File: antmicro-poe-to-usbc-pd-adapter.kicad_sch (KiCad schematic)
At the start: 91 parts, among them J1 Bus_RJ45_5-2337992-8, J2 Bus_RJ45_5-2337992-8, J3 USB-C_GCT_USB4105-GF-A, Q1 PJE138K, U1 TPS2372-3RGWR, U2 LV14540DDAR, U3 INA230AIRGTR, U4 IEA48003A280V-001-R, U5 FT4232H_VQFN, U6 TPS65987DDHRSHR, U7 LV14540DDAR, Y1 Resonator_12MHz_ABM8G

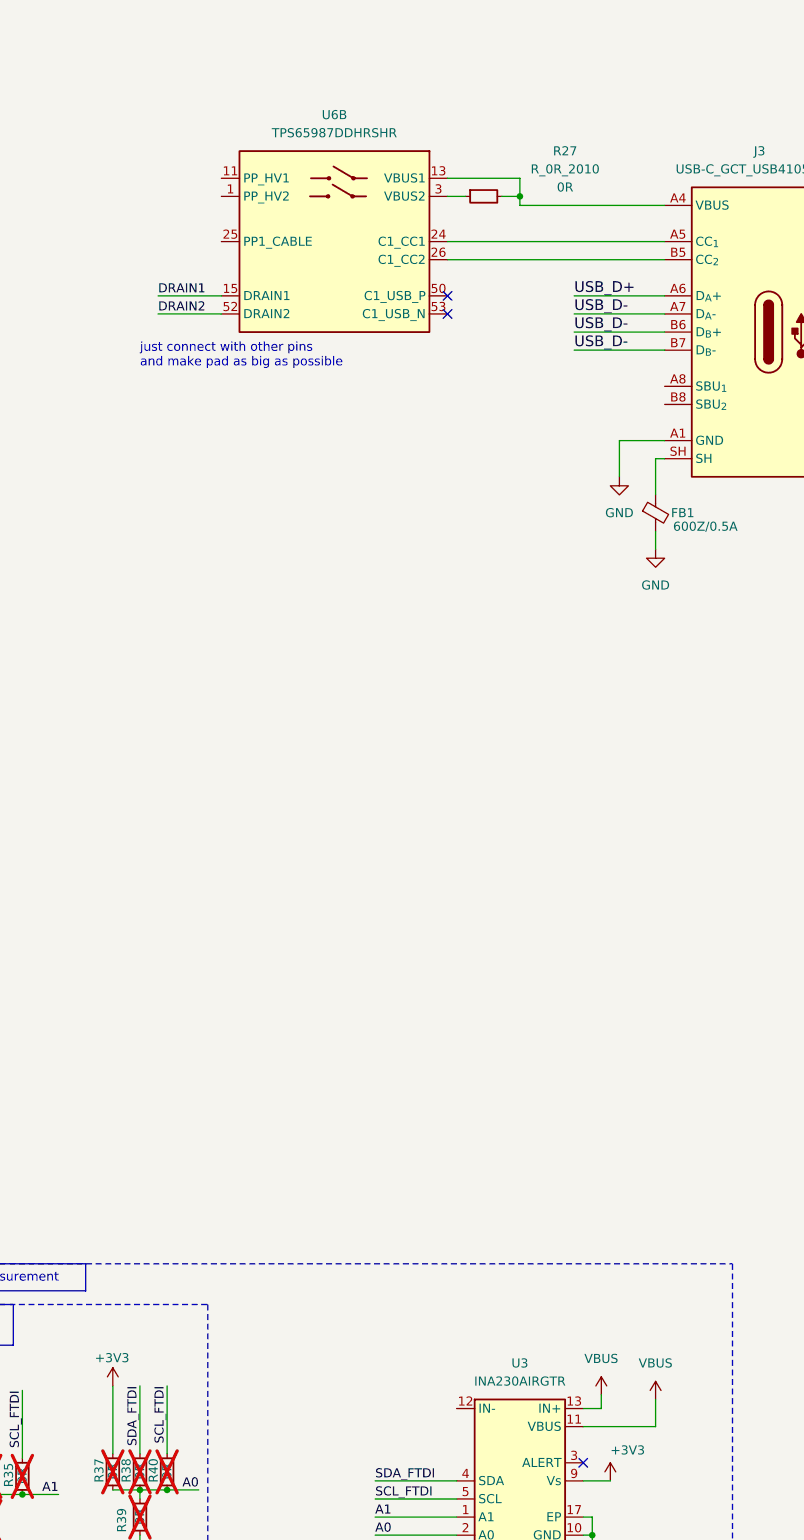
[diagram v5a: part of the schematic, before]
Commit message: [#62182] Add shunt resistor for INA230
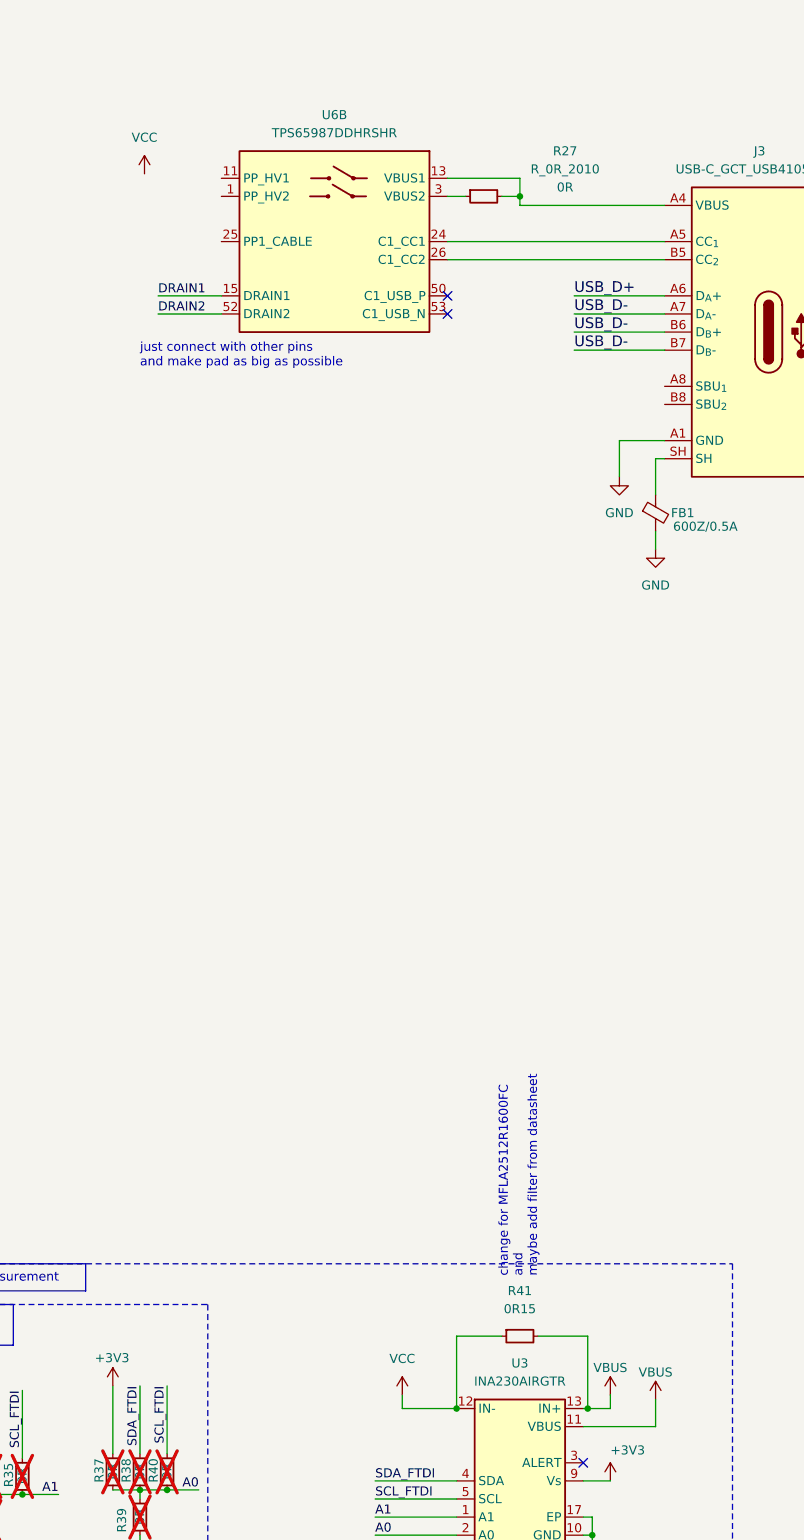
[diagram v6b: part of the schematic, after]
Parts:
- added R41: R_0R15_2010, antmicro-footprints:R_2010_5025Metric, symbol antmicroResistorsmisc:R_0R15_2010
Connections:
- net VBUS: now also R41.2
- net VCC: now reaches U3.12 (IN-)
- net VCC: now also R41.1
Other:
- note added: "change for MFLA2512R1600FC and maybe add filter from datasheet"
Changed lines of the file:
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@@
   (junction (at 367.03 111.125) (diameter 0) (color 0 0 0 0)
   )
+  (junction (at 358.14 281.305) (diameter 0) (color 0 0 0 0)
+  )
   (junction (at 133.35 353.06) (diameter 0) (color 0 0 0 0)
   )
@@
   (junction (at 189.23 361.95) (diameter 0) (color 0 0 0 0)
   )
+  (junction (at 376.555 281.305) (diameter 0) (color 0 0 0 0)
+  )
   (junction (at 133.35 379.73) (diameter 0) (color 0 0 0 0)
   )
@@
     (stroke (width 0) (type default))
   )
+  (wire (pts (xy 364.49 271.145) (xy 358.14 271.145))
+    (stroke (width 0) (type default))
+  )
   (wire (pts (xy 240.03 367.03) (xy 242.57 367.03))
     (stroke (width 0) (type default))
@@
     (stroke (width 0) (type default))
   )
+  (wire (pts (xy 376.555 281.305) (xy 379.73 281.305))
+    (stroke (width 0) (type default))
+  )
   (wire (pts (xy 292.735 299.72) (xy 292.735 300.99))
     (stroke (width 0) (type default))
@@
     (stroke (width 0) (type default))
   )
+  (wire (pts (xy 350.52 279.4) (xy 350.52 281.305))
+    (stroke (width 0) (type default))
+  )
   (wire (pts (xy 233.68 372.11) (xy 233.68 386.08))
     (stroke (width 0) (type default))
@@
     (stroke (width 0) (type default))
   )
+  (wire (pts (xy 358.14 271.145) (xy 358.14 281.305))
+    (stroke (width 0) (type default))
+  )
   (wire (pts (xy 115.57 334.01) (xy 123.19 334.01))
     (stroke (width 0) (type default))
@@
     (stroke (width 0) (type default))
   )
+  (wire (pts (xy 358.14 281.305) (xy 350.52 281.305))
+    (stroke (width 0) (type default))
+  )
   (wire (pts (xy 43.18 220.98) (xy 53.34 220.98))
     (stroke (width 0) (type default))
@@
     (stroke (width 0) (type default))
   )
-  (wire (pts (xy 378.46 279.4) (xy 378.46 281.305))
+  (wire (pts (xy 379.73 279.4) (xy 379.73 281.305))
     (stroke (width 0) (type default))
   )
@@
     (stroke (width 0) (type default))
   )
-  (wire (pts (xy 375.92 281.305) (xy 378.46 281.305))
+  (wire (pts (xy 375.92 281.305) (xy 376.555 281.305))
     (stroke (width 0) (type default))
   )
@@
     (stroke (width 0) (type default))
   )
+  (wire (pts (xy 376.555 281.305) (xy 376.555 271.145))
+    (stroke (width 0) (type default))
+  )
   (wire (pts (xy 27.94 332.74) (xy 27.94 328.93))
     (stroke (width 0) (type default))
@@
     (stroke (width 0) (type default))
   )
+  (wire (pts (xy 376.555 271.145) (xy 369.57 271.145))
+    (stroke (width 0) (type default))
+  )
   (wire (pts (xy 135.89 124.46) (xy 151.13 124.46))
     (stroke (width 0) (type default))
@@
     (effects (font (size 1.27 1.27)) (justify left bottom))
   )
+  (text "change for MFLA2512R1600FC\nand\nmaybe add filter from datasheet"
+    (at 369.57 262.89 90)
+    (effects (font (size 1.27 1.27)) (justify left bottom))
+  )
   (text "Nlogic same \nas Orin" (at 203.2 111.76 0)
     (effects (font (size 1.27 1.27)) (justify left bottom))
@@
     )
   )
-  (symbol (lib_id "antmicropower:VBUS") (at 378.46 279.4 0) (unit 1)
-    (in_bom yes) (on_board yes) (dnp no) (fields_autoplaced)
-    (property "Reference" "#PWR067" (at 378.46 283.21 0)
+  (symbol (lib_id "antmicropower:VBUS") (at 379.73 279.4 0) (unit 1)
+    (in_bom yes) (on_board yes) (dnp no)
+    (property "Reference" "#PWR067" (at 379.73 283.21 0)
       (effects (font (size 1.27 1.27)) hide)
     )
-    (property "Value" "VBUS" (at 378.46 274.32 0)
+    (property "Value" "VBUS" (at 379.73 275.59 0)
       (effects (font (size 1.27 1.27)))
     )
-    (property "Footprint" "" (at 378.46 279.4 0)
+    (property "Footprint" "" (at 379.73 279.4 0)
       (effects (font (size 1.27 1.27)) hide)
     )
-    (property "Datasheet" "" (at 378.46 279.4 0)
+    (property "Datasheet" "" (at 379.73 279.4 0)
       (effects (font (size 1.27 1.27)) hide)
     )
@@
     )
   )
+  (symbol (lib_id "antmicropower:VCC") (at 314.325 107.95 0) (unit 1)
+    (in_bom yes) (on_board yes) (dnp no) (fields_autoplaced)
+    (property "Reference" "#PWR068" (at 314.325 111.76 0)
+      (effects (font (size 1.27 1.27)) hide)
+    )
+    (property "Value" "VCC" (at 314.325 102.87 0)
+      (effects (font (size 1.27 1.27)))
+    )
+    (property "Footprint" "" (at 314.325 107.95 0)
+      (effects (font (size 1.27 1.27)) hide)
+    )
+    (property "Datasheet" "" (at 314.325 107.95 0)
+      (effects (font (size 1.27 1.27)) hide)
+    )
+    (pin "1")
+    (instances
+      (project "antmicro-poe-to-usbc-pd-adapter"
+        (path "/cf0d4429-3f03-449f-96a7-26d69371a46d"
+          (reference "#PWR068") (unit 1)
+        )
+      )
+    )
+  )
   (symbol (lib_name "R_0R_0402_2") (lib_id "antmicroResistors0402:R_0R_0402") (at 297.18 293.37 90) (unit 1)
     (in_bom yes) (on_board yes) (dnp yes)
@@
   )
   (symbol (lib_id "antmicropower:VBUS") (at 386.08 280.035 0) (unit 1)
-    (in_bom yes) (on_board yes) (dnp no) (fields_autoplaced)
+    (in_bom yes) (on_board yes) (dnp no)
     (property "Reference" "#PWR060" (at 386.08 283.845 0)
       (effects (font (size 1.27 1.27)) hide)
     )
-    (property "Value" "VBUS" (at 386.08 274.955 0)
+    (property "Value" "VBUS" (at 386.08 276.225 0)
       (effects (font (size 1.27 1.27)))
     )
@@
     )
   )
+  (symbol (lib_id "antmicropower:VCC") (at 350.52 279.4 0) (unit 1)
+    (in_bom yes) (on_board yes) (dnp no) (fields_autoplaced)
+    (property "Reference" "#PWR029" (at 350.52 283.21 0)
+      (effects (font (size 1.27 1.27)) hide)
+    )
+    (property "Value" "VCC" (at 350.52 274.32 0)
+      (effects (font (size 1.27 1.27)))
+    )
+    (property "Footprint" "" (at 350.52 279.4 0)
+      (effects (font (size 1.27 1.27)) hide)
+    )
+    (property "Datasheet" "" (at 350.52 279.4 0)
+      (effects (font (size 1.27 1.27)) hide)
+    )
+    (pin "1")
+    (instances
+      (project "antmicro-poe-to-usbc-pd-adapter"
+        (path "/cf0d4429-3f03-449f-96a7-26d69371a46d"
+          (reference "#PWR029") (unit 1)
+        )
+      )
+    )
+  )
   (symbol (lib_id "antmicroCapacitors0402:C_4u7_25V_0402") (at 48.26 228.6 90) (unit 1)
     (in_bom yes) (on_board yes) (dnp no)
@@
         )
       )
+    )
+  )
+  (symbol (lib_id "antmicroResistorsmisc:R_0R15_2010") (at 364.49 271.145 0) (unit 1)
+    (in_bom yes) (on_board yes) (dnp no) (fields_autoplaced)
+    (property "Reference" "R41" (at 367.03 264.795 0)
+      (effects (font (size 1.27 1.27) (thickness 0.15)))
+    )
+    (property "Value" "R_0R15_2010" (at 384.81 283.845 0)
+      (effects (font (size 1.27 1.27) (thickness 0.15)) (justify left bottom) hide)
+    )
+    (property "Footprint" "antmicro-footprints:R_2010_5025Metric" (at 384.81 286.385 0)
+      (effects (font (size 1.27 1.27) (thickness 0.15)) (justify left bottom) hide)
+    )
+    (property "Datasheet" "https://www.bourns.com/docs/product-datasheets/cr.pdf" (at 384.81 288.925 0)
+      (effects (font (size 1.27 1.27) (thickness 0.15)) (justify left bottom) hide)
+    )
+    (property "MPN" "CR2010-FX-0R15ELF" (at 384.81 291.465 0)
+      (effects (font (size 1.27 1.27) (thickness 0.15)) (justify left bottom) hide)
+    )
+    (property "Manufacturer" "Bourns" (at 384.81 294.005 0)
+      (effects (font (size 1.27 1.27) (thickness 0.15)) (justify left bottom) hide)
+    )
+    (property "License" "Apache-2.0" (at 384.81 296.545 0)
+      (effects (font (size 1.27 1.27) (thickness 0.15)) (justify left bottom) hide)
+    )
+    (property "Author" "Antmicro" (at 384.81 299.085 0)
+      (effects (font (size 1.27 1.27) (thickness 0.15)) (justify left bottom) hide)
+    )
+    (property "Val" "0R15" (at 367.03 267.335 0)
+      (effects (font (size 1.27 1.27) (thickness 0.15)))
+    )
+    (property "Tolerance" "1%" (at 384.81 281.305 0)
+      (effects (font (size 1.27 1.27)) (justify left bottom) hide)
+    )
+    (pin "2")
+    (pin "1")
+    (instances
+      (project "antmicro-poe-to-usbc-pd-adapter"
+        (path "/cf0d4429-3f03-449f-96a7-26d69371a46d"
+          (reference "R41") (unit 1)
+        )
+      )

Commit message: [#62182] Place components PCB
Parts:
- removed D5: PDS760, antmicro-footprints:PowerDI5, symbol antmicroDiodesRectifiersSingle:PDS760
- added C15: C_1u_25V_0402, antmicro-footprints:C_0402_1005Metric, symbol antmicroCapacitors0402:C_1u_25V_0402
- added D5: 1N5819HW-7-F, antmicro-footprints:D_SOD-123, symbol antmicroDiodesRectifiersSingle:1N5819HW-7-F
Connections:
- net GND: now also C15.1, D5.2 (A)
- net at C22.1, L2.1, U7.8 (SW): now also D5.1 (C)
- net at J3.A4 (VBUS), J3.A9 (VBUS), J3.B4 (VBUS)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: now also C15.2

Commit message: [#62182] Change R5
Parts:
- C2, R33, R34, R35, R36, R37, R38, R39, R40: DNP (none) -> DNP; now left out of the parts list
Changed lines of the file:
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@@
     (company "Antmicro ltd.")
   )
-  (bus_alias "CC" (members "CC1" "CC2"))
-  (bus_alias "ETH" (members "P1" "P2" "P3" "P6" "P7" "P8" "P9" "P10" "P4" "P5"))
-  (bus_alias "POE" (members "VC1" "VC2" "VC3" "VC4"))
   (junction (at 34.29 328.93) (diameter 0) (color 0 0 0 0)
   )
@@
     (stroke (width 0) (type default))
   )
+  (bus_alias "CC" (members "CC1" "CC2"))
+  (bus_alias "ETH" (members "P1" "P2" "P3" "P6" "P7" "P8" "P9" "P10" "P4" "P5"))
+  (bus_alias "POE" (members "VC1" "VC2" "VC3" "VC4"))
   (wire (pts (xy 317.5 292.735) (xy 321.945 292.735))
     (stroke (width 0) (type default))
@@
   )
   (symbol (lib_name "R_0R_0402_2") (lib_id "antmicroResistors0402:R_0R_0402") (at 317.5 292.735 90) (unit 1)
-    (in_bom yes) (on_board yes) (dnp yes)
+    (in_bom no) (on_board yes) (dnp yes)
     (property "Reference" "R40" (at 315.595 288.29 0)
       (effects (font (size 1.27 1.27) (thickness 0.15)) (justify right))
@@
       (effects (font (size 1.27 1.27) (thickness 0.15)) (justify left bottom) hide)
     )
+    (property "DNP" "DNP" (at 0.0 0.0 0)
+      (effects (font (size 1.0 1.0)))
+    )
     (pin "1")
     (pin "2")
@@
   )
   (symbol (lib_name "R_0R_0402_2") (lib_id "antmicroResistors0402:R_0R_0402") (at 292.735 299.72 90) (unit 1)
-    (in_bom yes) (on_board yes) (dnp yes)
+    (in_bom no) (on_board yes) (dnp yes)
     (property "Reference" "R36" (at 290.195 295.91 0)
       (effects (font (size 1.27 1.27) (thickness 0.15)) (justify right))
@@
       (effects (font (size 1.27 1.27) (thickness 0.15)) (justify left bottom) hide)
     )
+    (property "DNP" "DNP" (at 0.0 0.0 0)
+      (effects (font (size 1.0 1.0)))
+    )
     (pin "1")
     (pin "2")
@@
   )
   (symbol (lib_id "antmicroCapacitors0402:C_10n_50V_X7R_0402") (at 246.38 119.38 90) (unit 1)
-    (in_bom yes) (on_board yes) (dnp yes) (fields_autoplaced)
+    (in_bom no) (on_board yes) (dnp yes) (fields_autoplaced)
     (property "Reference" "C2" (at 248.92 115.5636 90)
       (effects (font (size 1.27 1.27) (thickness 0.15)) (justify right))
@@
       (effects (font (size 1.27 1.27) (thickness 0.15)) (justify left bottom) hide)
     )
+    (property "DNP" "DNP" (at 0.0 0.0 0)
+      (effects (font (size 1.0 1.0)))
+    )
     (pin "2")
     (pin "1")
@@
   )
   (symbol (lib_name "R_0R_0402_2") (lib_id "antmicroResistors0402:R_0R_0402") (at 297.18 293.37 90) (unit 1)
-    (in_bom yes) (on_board yes) (dnp yes)
+    (in_bom no) (on_board yes) (dnp yes)
     (property "Reference" "R35" (at 295.275 288.925 0)
       (effects (font (size 1.27 1.27) (thickness 0.15)) (justify right))
@@
       (effects (font (size 1.27 1.27) (thickness 0.15)) (justify left bottom) hide)
     )
+    (property "DNP" "DNP" (at 0.0 0.0 0)
+      (effects (font (size 1.0 1.0)))
+    )
     (pin "1")
     (pin "2")
@@
   )
   (symbol (lib_name "R_0R_0402_2") (lib_id "antmicroResistors0402:R_0R_0402") (at 313.69 299.085 90) (unit 1)
-    (in_bom yes) (on_board yes) (dnp yes)
+    (in_bom no) (on_board yes) (dnp yes)
     (property "Reference" "R39" (at 311.15 295.275 0)
       (effects (font (size 1.27 1.27) (thickness 0.15)) (justify right))
@@
       (effects (font (size 1.27 1.27) (thickness 0.15)) (justify left bottom) hide)
     )
+    (property "DNP" "DNP" (at 0.0 0.0 0)
+      (effects (font (size 1.0 1.0)))
+    )
     (pin "1")
     (pin "2")
@@
   )
   (symbol (lib_name "R_0R_0402_2") (lib_id "antmicroResistors0402:R_0R_0402") (at 288.925 293.37 90) (unit 1)
-    (in_bom yes) (on_board yes) (dnp yes)
+    (in_bom no) (on_board yes) (dnp yes)
     (property "Reference" "R33" (at 287.02 288.925 0)
       (effects (font (size 1.27 1.27) (thickness 0.15)) (justify right))
@@
       (effects (font (size 1.27 1.27) (thickness 0.15)) (justify left bottom) hide)
     )
+    (property "DNP" "DNP" (at 0.0 0.0 0)
+      (effects (font (size 1.0 1.0)))
+    )
     (pin "1")
     (pin "2")
@@
   )
   (symbol (lib_name "R_0R_0402_2") (lib_id "antmicroResistors0402:R_0R_0402") (at 313.69 292.735 90) (unit 1)
-    (in_bom yes) (on_board yes) (dnp yes)
+    (in_bom no) (on_board yes) (dnp yes)
     (property "Reference" "R38" (at 311.785 288.29 0)
       (effects (font (size 1.27 1.27) (thickness 0.15)) (justify right))
@@
       (effects (font (size 1.27 1.27) (thickness 0.15)) (justify left bottom) hide)
     )
+    (property "DNP" "DNP" (at 0.0 0.0 0)
+      (effects (font (size 1.0 1.0)))
+    )
     (pin "1")
     (pin "2")
@@
   )
   (symbol (lib_name "R_0R_0402_2") (lib_id "antmicroResistors0402:R_0R_0402") (at 309.88 292.735 90) (unit 1)
-    (in_bom yes) (on_board yes) (dnp yes)
+    (in_bom no) (on_board yes) (dnp yes)
     (property "Reference" "R37" (at 307.975 288.29 0)
       (effects (font (size 1.27 1.27) (thickness 0.15)) (justify right))
@@
       (effects (font (size 1.27 1.27) (thickness 0.15)) (justify left bottom) hide)
     )
+    (property "DNP" "DNP" (at 0.0 0.0 0)
+      (effects (font (size 1.0 1.0)))
+    )
     (pin "1")
     (pin "2")
@@
   )
   (symbol (lib_name "R_0R_0402_2") (lib_id "antmicroResistors0402:R_0R_0402") (at 292.735 293.37 90) (unit 1)
-    (in_bom yes) (on_board yes) (dnp yes)
+    (in_bom no) (on_board yes) (dnp yes)
     (property "Reference" "R34" (at 290.83 288.925 0)
       (effects (font (size 1.27 1.27) (thickness 0.15)) (justify right))
@@
       (effects (font (size 1.27 1.27) (thickness 0.15)) (justify left bottom) hide)
     )
+    (property "DNP" "DNP" (at 0.0 0.0 0)
+      (effects (font (size 1.0 1.0)))
+    )
     (pin "1")
